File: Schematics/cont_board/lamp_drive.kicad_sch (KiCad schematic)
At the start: 15 parts, among them J4 Conn_02x08_Counter_Clockwise, Q4 BD438, Q5 BD438, Q6 BD438, U1 ULN2803A, U2 ULN2803A, U3 MCP23017_SP

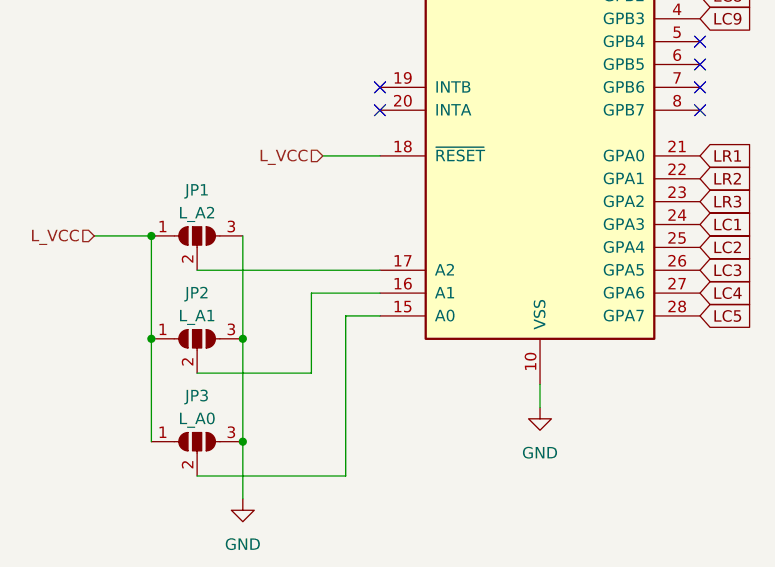
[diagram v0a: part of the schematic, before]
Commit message: Cont-board rev1.1 done and sent to manufacturing
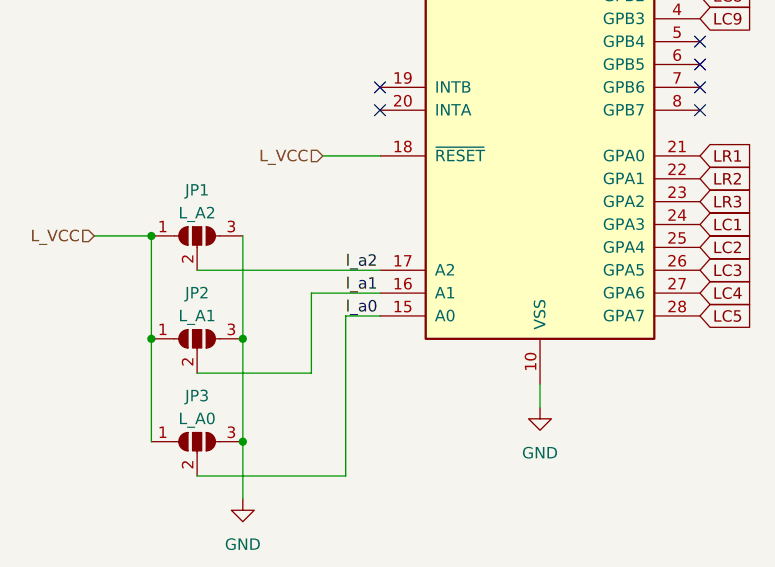
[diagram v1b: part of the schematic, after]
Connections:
- net l_a1: now reaches JP2.2 (C), U3.16 (A1)
- net l_a2: now reaches JP1.2 (C), U3.17 (A2)
- net l_a0: now reaches JP3.2 (C), U3.15 (A0)
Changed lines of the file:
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@@
+    (effects (font (size 1.27 1.27)) (justify left bottom))
+  )
+  (label "l_a2" (at 128.27 83.82 0) (fields_autoplaced)
     (effects (font (size 1.27 1.27)) (justify left bottom))
   )
@@
   )
   (label "c7" (at 265.43 55.88 0) (fields_autoplaced)
+    (effects (font (size 1.27 1.27)) (justify left bottom))
+  )
+  (label "l_a0" (at 128.27 88.9 0) (fields_autoplaced)
     (effects (font (size 1.27 1.27)) (justify left bottom))
   )
@@
     (effects (font (size 1.27 1.27)) (justify left bottom))
   )
+  (label "l_a1" (at 128.27 86.36 0) (fields_autoplaced)
+    (effects (font (size 1.27 1.27)) (justify left bottom))
+  )

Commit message: Final Commit
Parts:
- removed R2, R6: 4k7, Resistor_THT:R_Axial_DIN0207_L6.3mm_D2.5mm_P10.16mm_Horizontal, symbol Device:R
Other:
- company: (none) -> CUED
- title: (none) -> LZB23 - Enigma Control Board
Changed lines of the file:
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@@
 (kicad_sch (version 20230121) (generator eeschema)
   (paper "A4")
+  (title_block
+    (title "LZB23 - Enigma Control Board")
+    (rev "2.0")
+    (company "CUED")
+  )
   (junction (at 106.68 80.01) (diameter 0) (color 0 0 0 0)
   )
@@
   (junction (at 116.84 102.87) (diameter 0) (color 0 0 0 0)
   )
-  (junction (at 129.54 50.8) (diameter 0) (color 0 0 0 0)
-  )
-  (junction (at 127 48.26) (diameter 0) (color 0 0 0 0)
-  )
-  (junction (at 129.54 38.1) (diameter 0) (color 0 0 0 0)
-  )
   (junction (at 245.11 76.2) (diameter 0) (color 0 0 0 0)
   )
   (junction (at 116.84 91.44) (diameter 0) (color 0 0 0 0)
-  )
-  (junction (at 127 38.1) (diameter 0) (color 0 0 0 0)
   )
   (junction (at 228.6 76.2) (diameter 0) (color 0 0 0 0)
@@
     (stroke (width 0) (type default))
   )
-  (wire (pts (xy 125.73 48.26) (xy 127 48.26))
-    (stroke (width 0) (type default))
-  )
   (wire (pts (xy 219.71 90.17) (xy 236.22 90.17))
     (stroke (width 0) (type default))
@@
     (stroke (width 0) (type default))
   )
-  (wire (pts (xy 127 38.1) (xy 129.54 38.1))
-    (stroke (width 0) (type default))
-  )
   (wire (pts (xy 224.79 113.03) (xy 276.86 113.03))
     (stroke (width 0) (type default))
@@
     (stroke (width 0) (type default))
   )
-  (wire (pts (xy 127 45.72) (xy 127 48.26))
-    (stroke (width 0) (type default))
-  )
   (wire (pts (xy 111.76 95.25) (xy 124.46 95.25))
     (stroke (width 0) (type default))
@@
     (stroke (width 0) (type default))
   )
-  (wire (pts (xy 129.54 45.72) (xy 129.54 50.8))
-    (stroke (width 0) (type default))
-  )
   (wire (pts (xy 238.76 63.5) (xy 252.73 63.5))
     (stroke (width 0) (type default))
   )
-  (wire (pts (xy 129.54 50.8) (xy 132.08 50.8))
+  (wire (pts (xy 125.73 50.8) (xy 132.08 50.8))
     (stroke (width 0) (type default))
   )
@@
     (stroke (width 0) (type default))
   )
-  (wire (pts (xy 125.73 50.8) (xy 129.54 50.8))
-    (stroke (width 0) (type default))
-  )
   (wire (pts (xy 265.43 55.88) (xy 274.32 55.88))
     (stroke (width 0) (type default))
@@
     (stroke (width 0) (type default))
   )
-  (wire (pts (xy 120.65 38.1) (xy 127 38.1))
+  (wire (pts (xy 120.65 38.1) (xy 149.86 38.1))
     (stroke (width 0) (type default))
   )
@@
     (stroke (width 0) (type default))
   )
-  (wire (pts (xy 127 48.26) (xy 132.08 48.26))
+  (wire (pts (xy 125.73 48.26) (xy 132.08 48.26))
     (stroke (width 0) (type default))
   )
   (wire (pts (xy 226.06 111.76) (xy 275.59 111.76))
-    (stroke (width 0) (type default))
-  )
-  (wire (pts (xy 129.54 38.1) (xy 149.86 38.1))
     (stroke (width 0) (type default))
   )
@@
         (path "/c1253333-69bd-4894-a257-a3518ad25b0f/68818f13-e571-4b23-820a-6119b016610e"
           (reference "#PWR013") (unit 1)
-        )
-      )
-    )
-  )
-  (symbol (lib_id "Device:R") (at 129.54 41.91 0) (mirror y) (unit 1)
-    (in_bom yes) (on_board yes) (dnp no) (fields_autoplaced)
-    (property "Reference" "R6" (at 132.08 41.275 0)
-      (effects (font (size 1.27 1.27)) (justify right))
-    )
-    (property "Value" "4k7" (at 132.08 43.815 0)
-      (effects (font (size 1.27 1.27)) (justify right))
-    )
-    (property "Footprint" "Resistor_THT:R_Axial_DIN0207_L6.3mm_D2.5mm_P10.16mm_Horizontal" (at 131.318 41.91 90)
-      (effects (font (size 1.27 1.27)) hide)
-    )
-    (property "Datasheet" "~" (at 129.54 41.91 0)
-      (effects (font (size 1.27 1.27)) hide)
-    )
-    (pin "1")
-    (pin "2")
-    (instances
-      (project "cont_board"
-        (path "/c1253333-69bd-4894-a257-a3518ad25b0f"
-          (reference "R6") (unit 1)
-        )
-        (path "/c1253333-69bd-4894-a257-a3518ad25b0f/68818f13-e571-4b23-820a-6119b016610e"
-          (reference "R7") (unit 1)
         )
       )
@@
         )
       )
-    )
-  )
-  (symbol (lib_id "Device:R") (at 127 41.91 0) (unit 1)
-    (in_bom yes) (on_board yes) (dnp no) (fields_autoplaced)
-    (property "Reference" "R2" (at 124.46 41.275 0)
-      (effects (font (size 1.27 1.27)) (justify right))
-    )
-    (property "Value" "4k7" (at 124.46 43.815 0)
-      (effects (font (size 1.27 1.27)) (justify right))
-    )
-    (property "Footprint" "Resistor_THT:R_Axial_DIN0207_L6.3mm_D2.5mm_P10.16mm_Horizontal" (at 125.222 41.91 90)
-      (effects (font (size 1.27 1.27)) hide)
-    )
-    (property "Datasheet" "~" (at 127 41.91 0)
-      (effects (font (size 1.27 1.27)) hide)
-    )
-    (pin "1")
-    (pin "2")
-    (instances
-      (project "cont_board"
-        (path "/c1253333-69bd-4894-a257-a3518ad25b0f"
-          (reference "R2") (unit 1)
-        )
-        (path "/c1253333-69bd-4894-a257-a3518ad25b0f/68818f13-e571-4b23-820a-6119b016610e"
-          (reference "R6") (unit 1)
-        )
-      )
